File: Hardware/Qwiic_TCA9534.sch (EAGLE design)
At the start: 24 parts, among them J2 SMD, J3 PTH, J4 SMD

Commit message: fixing silk, move resistors from mounting holes
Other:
- note added: "dddd"
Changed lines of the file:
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@@
 <text x="165.1" y="175.26" size="1.27" layer="97">keypad only needs 7 gpio
 board can provide up to 8 gpio</text>
+<text x="91.44" y="109.22" size="1.27" layer="91">dddd</text>
 </plain>
 <instances>

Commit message: partial route
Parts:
- removed J8: (no value), SparkFun-Connectors:CONN_10NO_SILK_PTH_FEMALE
- added J5: (no value), SparkFun-Connectors:CONN_08NO_SILK_FEMALE_PTH
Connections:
- removed net 2: J8.3, U$3.P1
- removed net SCL/SCK/RX: J2.SCL, J3.SCL, J4.SCL
- removed net SDA/MISO/TX: J2.SDA, J3.SDA, J4.SDA
- new net P1: J5.2, U$3.P1
- net GND: no longer J8.1, J8.10
- net P0: now also J5.1; no longer J8.2
- net P2: now also J5.3; no longer J8.4
- net P3: now also J5.4; no longer J8.5
- net P4: now also J5.5; no longer J8.6
- net P5: now also J5.6; no longer J8.7
- net P6: now also J5.7; no longer J8.8
- net P7: now also J5.8; no longer J8.9
- net SCL: now also J2.SCL, J3.SCL, J4.SCL, R4.1
- net SDA: now also J2.SDA, J3.SDA, J4.SDA, R2.1
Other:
- note removed: "dddd"
- moved on the sheet: R2, R4, SJ5, U$3

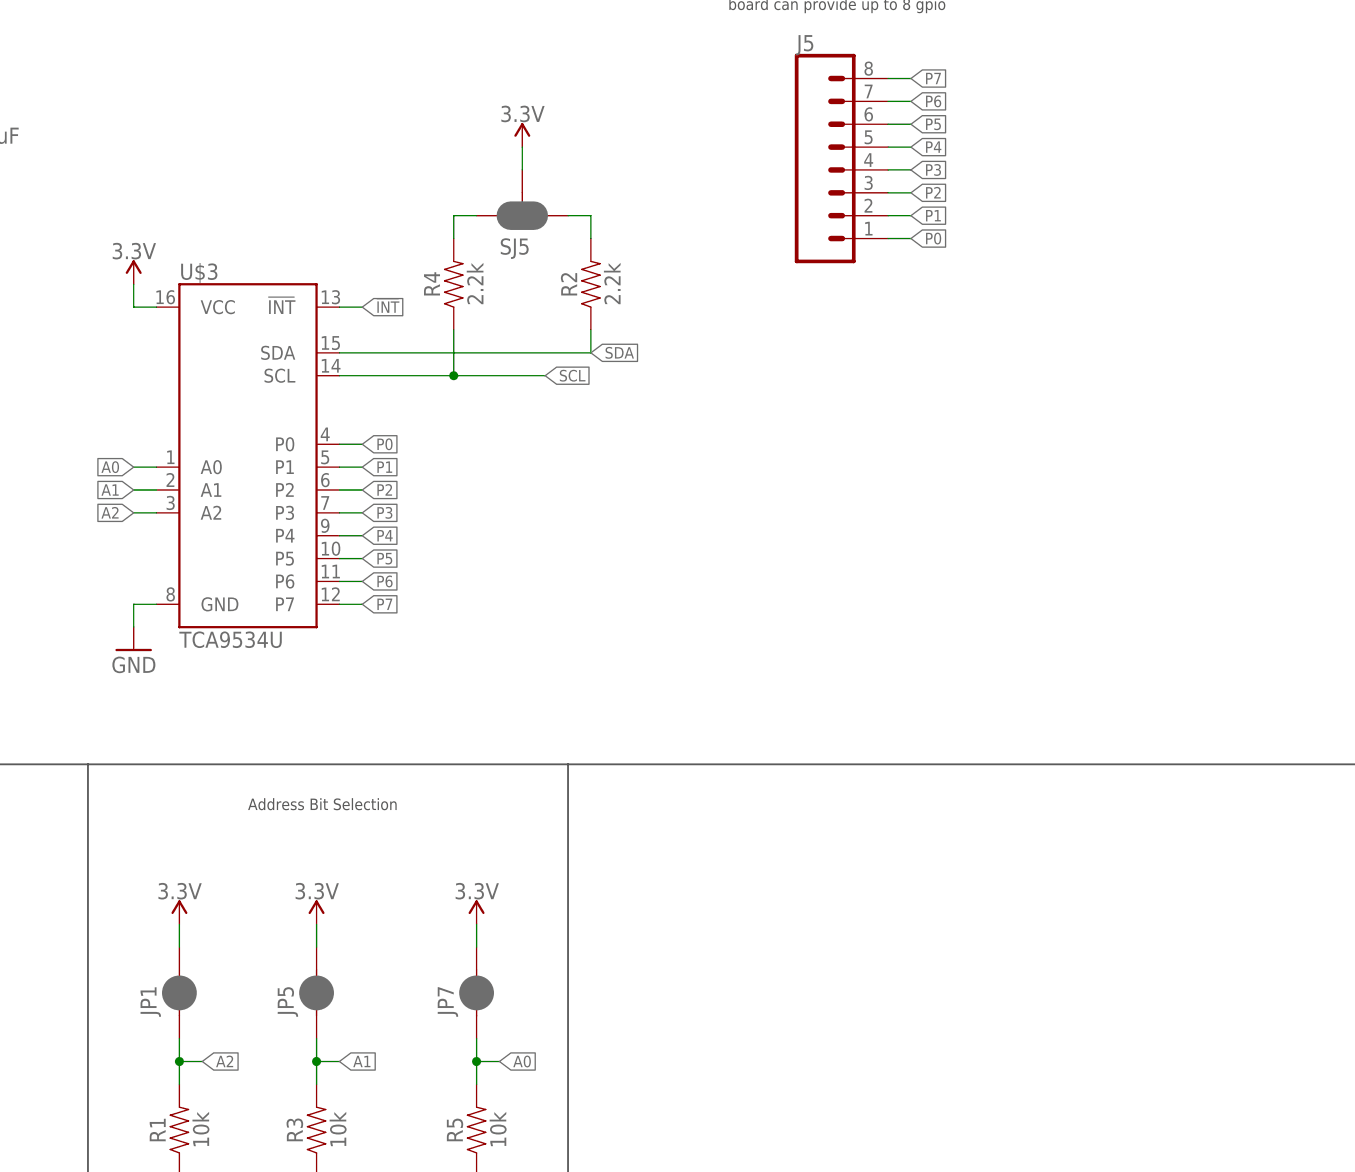
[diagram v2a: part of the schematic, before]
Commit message: starting to build out example 1
example 1 is to set a pin on the expander as output or input, then set it as high or low. currently the setPinMode() function works, next is to make a 'digitalWrite' equivalent
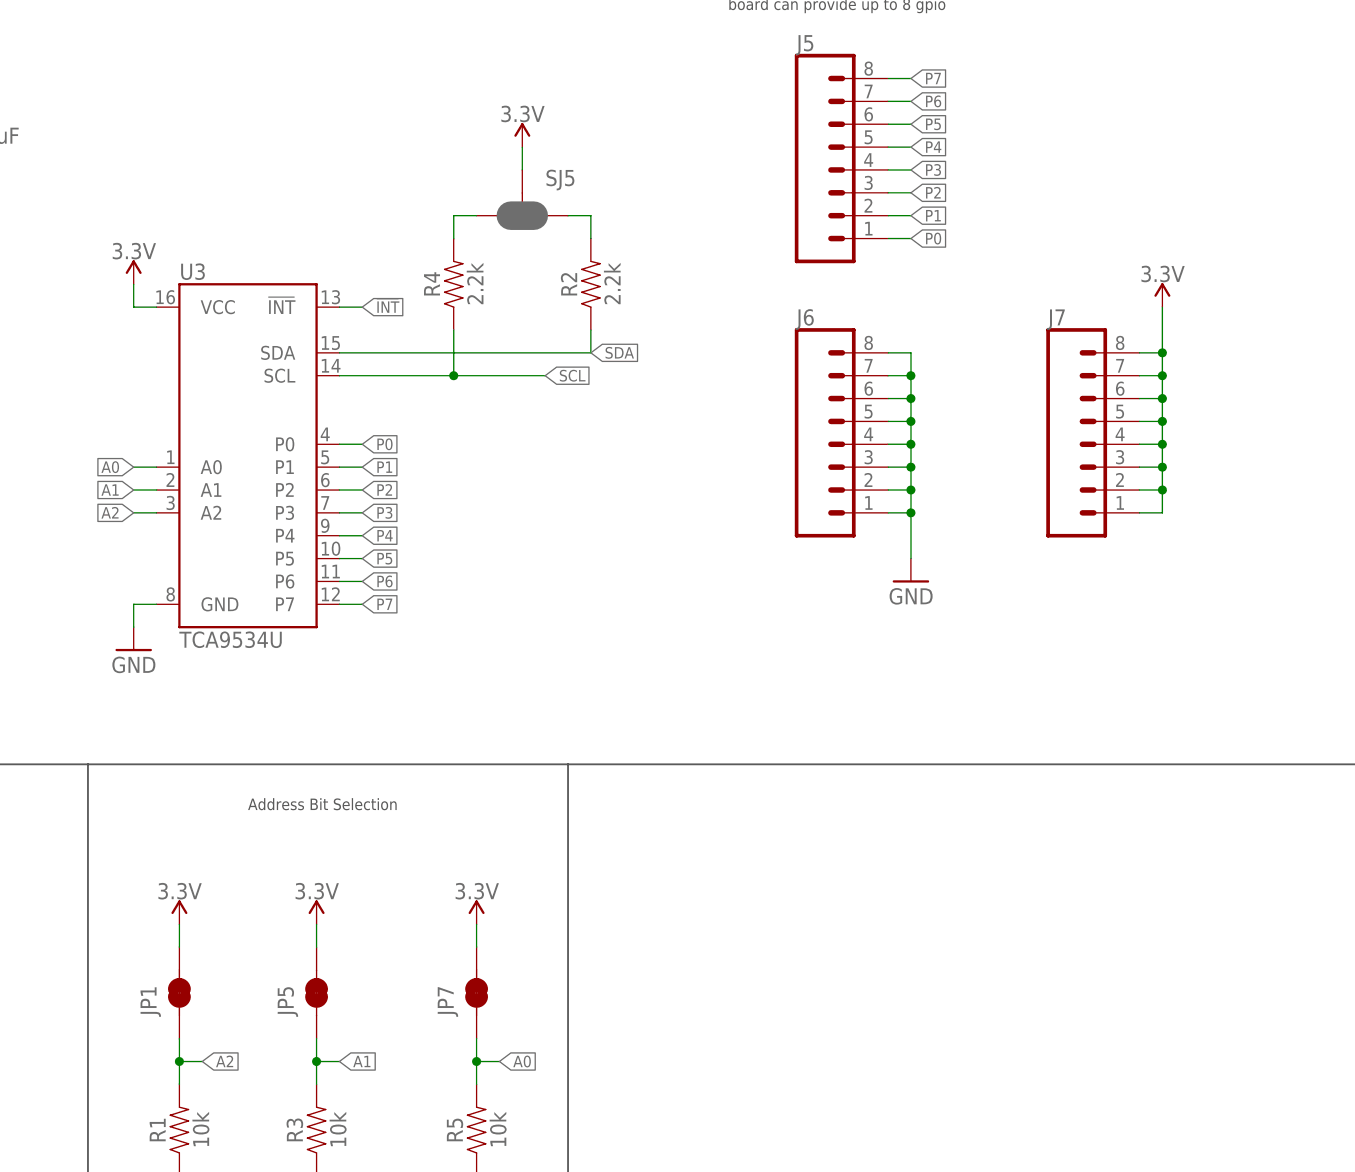
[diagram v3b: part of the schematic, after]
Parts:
- added J6, J7: (no value), SparkFun-Connectors:CONN_08NO_SILK_FEMALE_PTH
- JP1, JP5, JP7: value JUMPER-SMT_2_NC_PASTE_NO-SILK -> JUMPER-SMT_2_NC_TRACE_NO-SILK; device SparkFun-Jumpers:JUMPER-SMT_2_NC_PASTE_NO-SILK -> SparkFun-Jumpers:JUMPER-SMT_2_NC_TRACE_NO-SILK
- SJ5: value JUMPER-SMT_3_2-NC_PASTE_SILK -> SMT-JUMPER-_3-2-NC-PASTE_TALL; device SparkFun-Jumpers:JUMPER-SMT_3_2-NC_PASTE_SILK -> KevinKuwata_eagle:SMT-JUMPER-_3-2-NC-PASTE_TALL
- renumbered U$3 to U3
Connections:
- net 3.3V: now also J7.1, J7.2, J7.3, J7.4, J7.5, J7.6, J7.7, J7.8
- net GND: now also J6.1, J6.2, J6.3, J6.4, J6.5, J6.6, J6.7, J6.8
